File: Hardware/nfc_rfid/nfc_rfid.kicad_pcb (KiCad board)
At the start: 4 copper layers, 74.1 x 32 mm, 158 parts, among them IC1 ST25R3916-AQWT, IC2 FAN48610BUC50X, J1 BW0033AG-L3.4W0.9H1.8, J2 BW0033AG-L3.4W0.9H1.8, J3 HC-FPC-05-09-18RLTAG, J4 +, J5 -, J6 AFH34-S06FIA-1H, J7 BW0033AG-L3.4W0.9H1.8, J8 BW0033AG-L3.4W0.9H1.8, Q1 AO3400A, Q2 DMN2004TK-7, Q3 DMP2004TK-7, Q4 DMN2004TK-7, Q5 DMN5L06TK-7, U1 LMV358AIDGKR, U2 LMV331IDCKR, U3 LMV358AIDGKR, Y1 CF4027M12010001

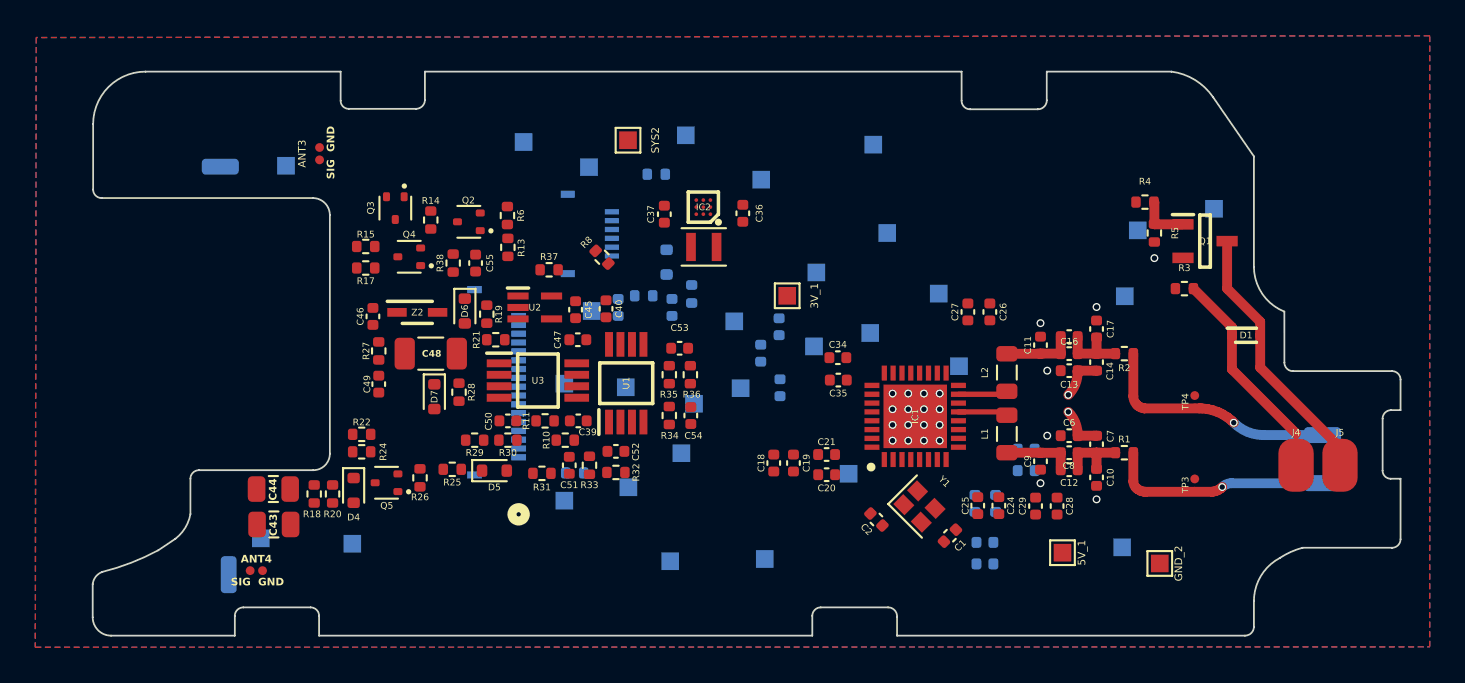
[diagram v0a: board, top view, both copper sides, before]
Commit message: PCB: RFID low freq part done
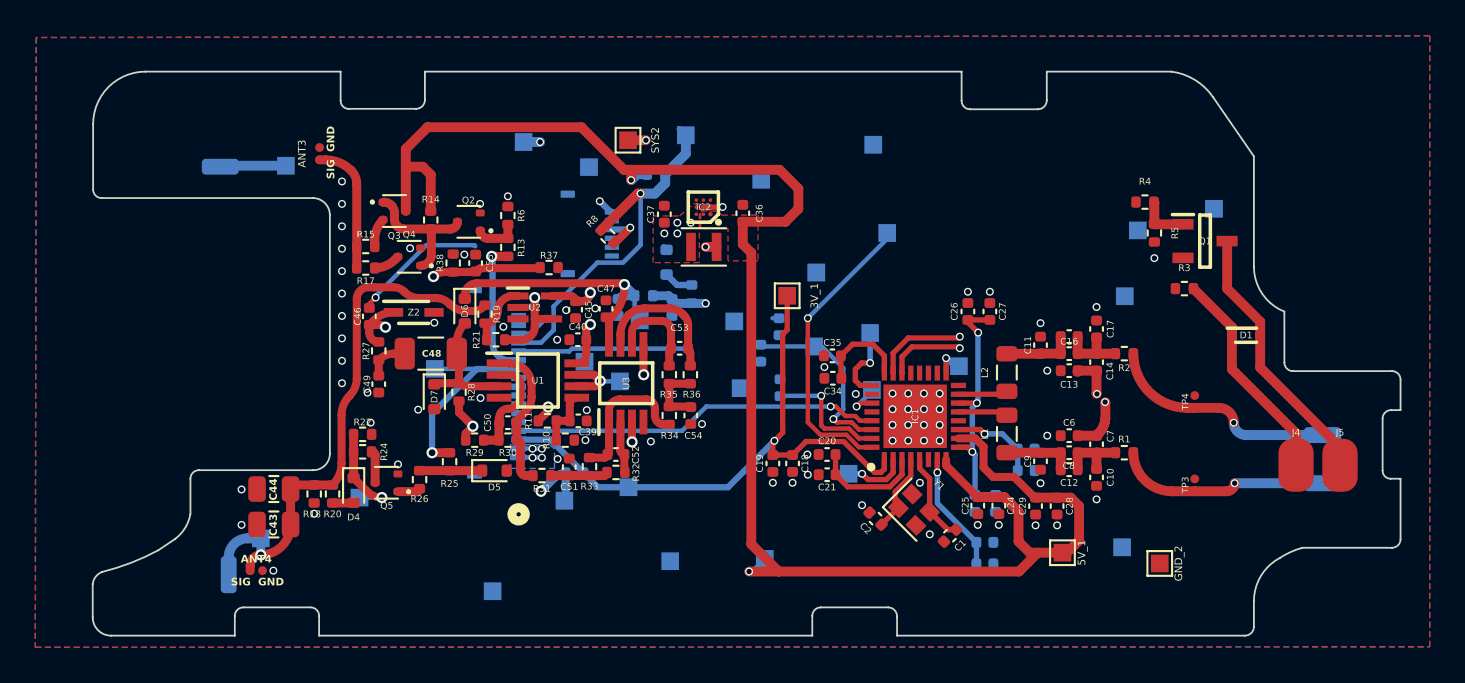
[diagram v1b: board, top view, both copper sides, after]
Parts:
- moved TP16 13.2 mm to (94.2, 76.9)
- moved TP12 7.39 mm to (91.0, 64.3)
- moved TP40 6.64 mm to (115.7, 65.5)
- moved TP15 6.64 mm to (99.4, 63.9)
- moved U1 5.01 mm to (96.8, 65.0), turned to 0 degrees
- moved U3 5.01 mm to (101.8, 65.2), turned to 90 degrees
- moved TP34 2.77 mm to (102.6, 61.6)
- moved TP39 2.65 mm to (86.7, 71.6)
- moved C40 2.37 mm to (99.1, 62.7), turned to 0 degrees
- moved C47 2.37 mm to (100.7, 60.9), turned to -90 degrees
- moved C35 1.41 mm to (113.5, 63.6), turned to 180 degrees
- moved C26 1.24 mm to (121.2, 61.1), turned to 90 degrees
- moved C27 1.24 mm to (122.4, 61.1), turned to 90 degrees
- moved R8 1.24 mm to (100.8, 56.8)
- moved C34 1.20 mm to (113.5, 64.9), turned to 180 degrees
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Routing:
- net +5V: track 0.00 -> 98.5 mm, vias 0 -> 2
- net /Peripheral/RFID_CARRIER: track 0.00 -> 46.6 mm, vias 0 -> 4
- net +3.3V: track 0.00 -> 46.6 mm, vias 0 -> 2
- net Net-(J7-Pin_1): track 0.00 -> 31.6 mm, vias 0 -> 1
- net A+3.3V: track 0.00 -> 29.5 mm, vias 0 -> 4
- net /Peripheral/iBTN: track 0.00 -> 29.0 mm, vias 0 -> 2
- net /NFC/NFC_CS: track 0.00 -> 20.9 mm, vias 0 -> 1
- net +1.65V: track 0.00 -> 17.9 mm, vias 0 -> 4
- net /NFC/SPI_R_MISO: track 0.00 -> 17.2 mm, vias 0 -> 1
- net /NFC/SPI_R_MOSI: track 0.00 -> 17.0 mm, vias 0 -> 1
- net /NFC/RFI_P: track 2.55 -> 17.8 mm, vias 1 -> 2
- net /NFC/RFI_N: track 2.65 -> 17.6 mm, vias 1 -> 2
- net Net-(IC1-VDD_DR): track 0.00 -> 14.7 mm, vias 0 -> 3
- net /Peripheral/RFID_PULL: track 0.00 -> 11.5 mm, vias 0 -> 1
- net Net-(J8-Pin_1): track 0.00 -> 11.3 mm
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- added copper zone on In1.Cu, net +1.65V
- added copper zone on F.Cu, net +5V
- added copper zone on In1.Cu, net A+3.3V
- added copper zone on B.Cu, net SYS
- added copper zone on F.Cu, net SYS
- added copper zone on In1.Cu, net SYS

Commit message: PCB: NFC_RFID layout done
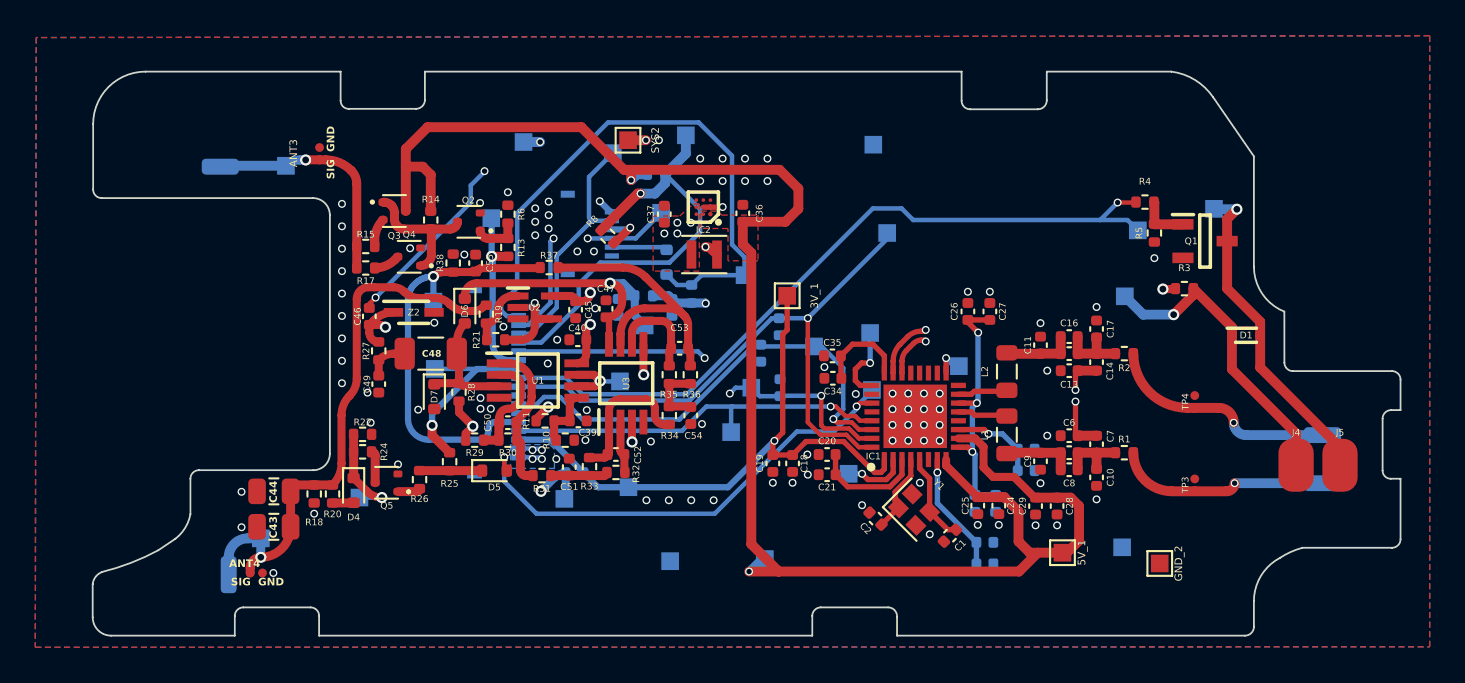
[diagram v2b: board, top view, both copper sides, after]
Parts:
- IC2: value FAN48610BUC50X -> FAN48610UC50X
- moved TP16 16.2 mm to (107.7, 67.9)
- moved TP11 15.0 mm to (94.2, 55.8)
- moved TP15 9.21 mm to (90.9, 60.5)
- moved TP7 5.97 mm to (103.8, 55.5)
- moved TP6 4.07 mm to (108.5, 59.0)
- moved TP8 1.56 mm to (101.0, 52.1)
- moved TP10 0.61 mm to (108.9, 65.4)
- moved L3 0.43 mm to (106.2, 57.9)
- moved TP34 0.40 mm to (102.8, 61.9)
- moved C44 0.13 mm to (81.8, 71.3)
- moved TP38 0.13 mm to (80.8, 75.9)
- moved C43 0.13 mm to (81.8, 73.3)
- moved R11 0.13 mm to (97.2, 67.3)
- moved TP18 0.10 mm to (98.3, 71.7)
- moved R19 0.08 mm to (93.9, 61.2)
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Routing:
- net Net-(J3-Pad10): track 0.00 -> 42.8 mm, vias 0 -> 1
- net /Peripheral/IR_RX: track 1.67 -> 34.0 mm
- net /NFC/NFC_IRQ: track 2.24 -> 27.8 mm, vias 1 -> 2
- net /NFC/SPI_R_MISO: track 17.2 -> 35.4 mm
- net /Peripheral/RFID_RF_IN: track 6.18 -> 24.0 mm
- net /Peripheral/iBTN: track 29.0 -> 45.5 mm, vias 2 -> 3
- net /NFC/SPI_R_SCK: track 10.9 -> 27.0 mm
- net /RFID_iBTN/IR_TX: track 0.00 -> 12.8 mm, vias 0 -> 2
- net /RFID_iBTN/SPEAKER: track 2.02 -> 14.1 mm
- net Net-(C53-Pad2): track 8.07 -> 16.3 mm
- net /NFC/SPI_R_MOSI: track 17.0 -> 24.6 mm, vias 1 -> 3
- net Net-(D1-K): track 12.4 -> 17.6 mm, vias 0 -> 1
- net Net-(D1-A): track 15.3 -> 18.7 mm, vias 0 -> 1
- net /RFID_iBTN/TSOP_RX: track 0.21 -> 3.16 mm
- net /NFC/RFI_P: track 17.8 -> 15.4 mm
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- added copper zone on In2.Cu, net +1.65V
- added copper zone on In2.Cu, net A+3.3V
- added copper zone on In1.Cu, net GND
- added copper zone on In2.Cu, net SYS
- removed copper zone on In1.Cu, net +1.65V
- removed copper zone on In1.Cu, net A+3.3V
- removed copper zone on In2.Cu, net GND
- removed copper zone on In1.Cu, net SYS

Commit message: PCB: nfc_rfid add via
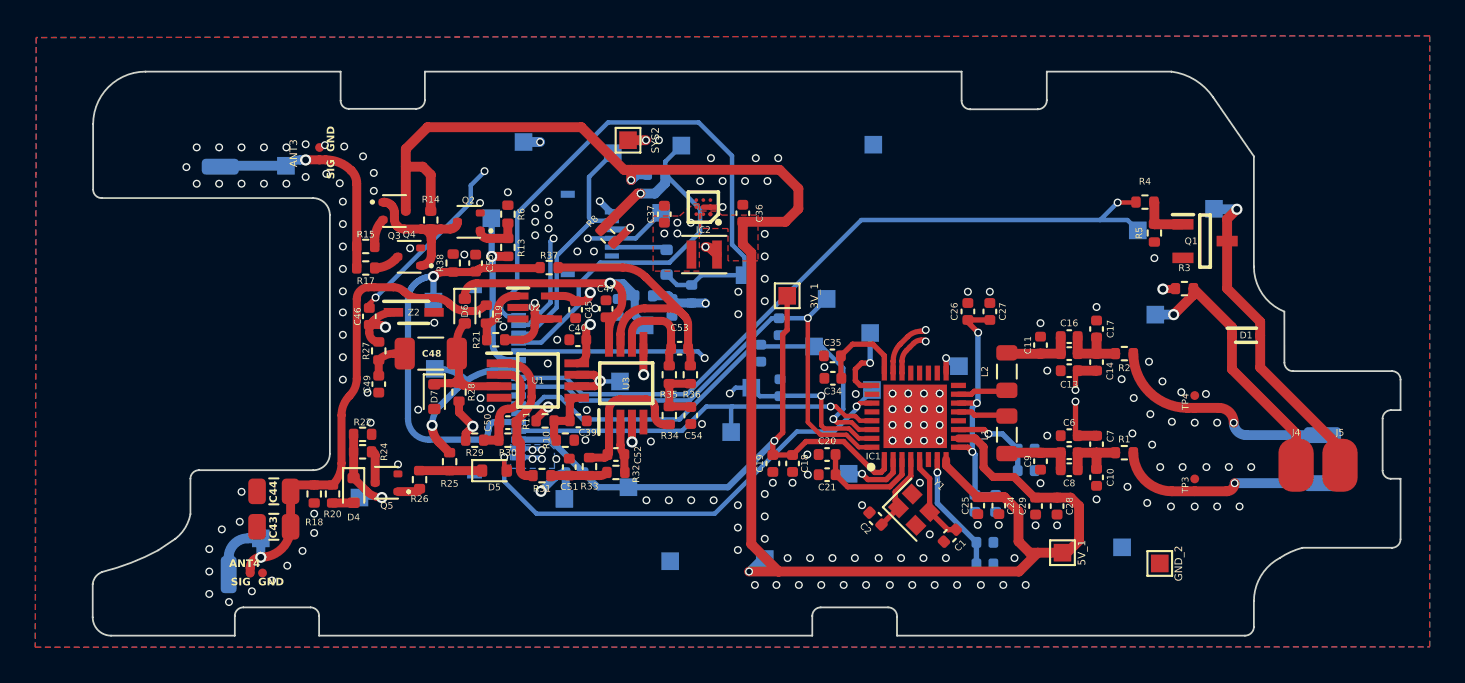
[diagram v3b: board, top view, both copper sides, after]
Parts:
- moved TP13 5.07 mm to (113.2, 60.4)
- moved TP21 2.02 mm to (131.8, 61.3)
- moved TP9 0.64 mm to (104.9, 51.7)
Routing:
- net /NFC/SPI_R_MISO: track 35.4 -> 30.3 mm
- net Net-(D1-K): track 17.6 -> 15.5 mm
- net Net-(Q2-D): track 7.87 -> 9.79 mm
- net Net-(D6-A): track 7.26 -> 9.16 mm
- net /Peripheral/RFID_CARRIER: track 46.1 -> 47.3 mm
- net A+3.3V: track 30.4 -> 31.6 mm
- net /Peripheral/RFID_PULL: track 11.0 -> 10.2 mm
- net /Peripheral/iBTN: track 45.5 -> 44.8 mm
- net Net-(J3-Pad10): track 42.8 -> 42.3 mm
- net GND: vias 93 -> 178

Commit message: PCB: add "remove from bom" entity; adjust design rule
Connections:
- J3 pad 19: (no net) -> GND
- J3 pad 20: (no net) -> GND
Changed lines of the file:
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@@
 		(sheetname "NFC")
 		(sheetfile "nfc.kicad_sch")
-		(attr smd)
+		(attr smd exclude_from_bom)
 		(fp_text user "${REFERENCE}"
 			(at 0 -3.3782 90)
@@
 		(sheetname "Peripheral")
 		(sheetfile "peripheral.kicad_sch")
-		(attr exclude_from_pos_files)
+		(attr exclude_from_pos_files exclude_from_bom)
 		(fp_line
 			(start 0.7 -0.7)
@@
 		(sheetname "NFC")
 		(sheetfile "nfc.kicad_sch")
-		(attr smd)
+		(attr smd exclude_from_bom)
 		(fp_text user "${REFERENCE}"
 			(at 0 -3.3782 90)
@@
 		(sheetname "Peripheral")
 		(sheetfile "peripheral.kicad_sch")
-		(attr exclude_from_pos_files)
+		(attr exclude_from_pos_files exclude_from_bom)
 		(fp_line
 			(start 0.7 -0.7)
@@
 		(sheetname "RFID_iBTN")
 		(sheetfile "RFID_iBTN.kicad_sch")
-		(attr smd)
+		(attr smd exclude_from_bom)
 		(fp_text user "${REFERENCE}"
 			(at 0 -3.3782 90)
@@
 		(sheetname "Peripheral")
 		(sheetfile "peripheral.kicad_sch")
-		(attr exclude_from_pos_files)
+		(attr exclude_from_pos_files exclude_from_bom)
 		(fp_line
 			(start 0.7 -0.7)
@@
 		(sheetname "Peripheral")
 		(sheetfile "peripheral.kicad_sch")
-		(attr exclude_from_pos_files)
+		(attr exclude_from_pos_files exclude_from_bom)
 		(fp_line
 			(start 0.7 -0.7)
@@
 		(sheetname "RFID_iBTN")
 		(sheetfile "RFID_iBTN.kicad_sch")
-		(attr smd)
+		(attr smd exclude_from_bom)
 		(fp_text user "${REFERENCE}"
 			(at 0 -3.3782 0)
@@
 			)
 		)
-		(property "Datasheet" ""
+		(property "Datasheet" "https://datasheet.datasheetarchive.com/originals/distributors/Datasheets_SAMA/df3e85b90ab3bcbb613a20fbddbf2a27.pdf"
 			(at 0 0 0)
 			(layer "F.Fab")
@@
 			)
 		)
-		(property "Mouser Part Number" ""
+		(property "Mouser Part Number" "512-FAN48610BUC50X"
 			(at 0 0 180)
 			(unlocked yes)
@@
 			)
 		)
-		(property "Manufacturer_Part_Number" "FAN48610UC50X"
+		(property "Manufacturer_Part_Number" "FAN48610BUC50X"
 			(at 0 0 180)
 			(unlocked yes)
@@
 		(sheetname "Peripheral")
 		(sheetfile "peripheral.kicad_sch")
-		(attr exclude_from_pos_files)
+		(attr exclude_from_pos_files exclude_from_bom)
 		(fp_line
 			(start 0.7 0.7)
@@
 		(sheetname "NFC")
 		(sheetfile "nfc.kicad_sch")
-		(attr exclude_from_pos_files)
+		(attr exclude_from_pos_files exclude_from_bom)
 		(fp_line
 			(start 0.7 0.7)
@@
 		(sheetname "Peripheral")
 		(sheetfile "peripheral.kicad_sch")
-		(attr exclude_from_pos_files)
+		(attr exclude_from_pos_files exclude_from_bom)
 		(fp_line
 			(start 0.7 0.7)
@@
 		(sheetname "RFID_iBTN")
 		(sheetfile "RFID_iBTN.kicad_sch")
-		(attr exclude_from_pos_files)
+		(attr exclude_from_pos_files exclude_from_bom)
 		(fp_line
 			(start 0.7 0.7)
@@
 		(sheetname "Peripheral")
 		(sheetfile "peripheral.kicad_sch")
-		(attr exclude_from_pos_files)
+		(attr exclude_from_pos_files exclude_from_bom)
 		(fp_line
 			(start 0.7 0.7)
@@
 		(sheetname "Peripheral")
 		(sheetfile "peripheral.kicad_sch")
-		(attr exclude_from_pos_files)
+		(attr exclude_from_pos_files exclude_from_bom)
 		(fp_line
 			(start 0.7 0.7)
@@
 		(sheetname "Peripheral")
 		(sheetfile "peripheral.kicad_sch")
-		(attr exclude_from_pos_files)
+		(attr exclude_from_pos_files exclude_from_bom)
 		(fp_line
 			(start 0.7 0.7)
@@
 			(size 0.4064 0.8382)
 			(layers "B.Cu" "B.Paste" "B.Mask")
+			(net 1 "GND")
+			(pinfunction "19")
+			(pintype "passive")
 		)
 		(pad "20" smd rect
@@
 			(size 0.4064 0.8382)
 			(layers "B.Cu" "B.Paste" "B.Mask")
+			(net 1 "GND")
+			(pinfunction "20")
+			(pintype "passive")
 		)
 	)
@@
 		(sheetname "Peripheral")
 		(sheetfile "peripheral.kicad_sch")
-		(attr exclude_from_pos_files)
+		(attr exclude_from_pos_files exclude_from_bom)
 		(fp_line
 			(start 0.7 0.7)
@@
 		(sheetname "Peripheral")
 		(sheetfile "peripheral.kicad_sch")
-		(attr exclude_from_pos_files)
+		(attr exclude_from_pos_files exclude_from_bom)
 		(fp_line
 			(start 0.7 0.7)
@@
 		(sheetname "RFID_iBTN")
 		(sheetfile "RFID_iBTN.kicad_sch")
-		(attr exclude_from_pos_files)
+		(attr exclude_from_pos_files exclude_from_bom)
 		(fp_line
 			(start -0.7 0.7)
@@
 		(sheetname "RFID_iBTN")
 		(sheetfile "RFID_iBTN.kicad_sch")
-		(attr exclude_from_pos_files)
+		(attr exclude_from_pos_files exclude_from_bom)
 		(fp_line
 			(start -0.7 0.7)
@@
 		(sheetname "Peripheral")
 		(sheetfile "peripheral.kicad_sch")
-		(attr exclude_from_pos_files)
+		(attr exclude_from_pos_files exclude_from_bom)
 		(fp_line
 			(start 0.7 0.7)
@@
 		(sheetname "Peripheral")
 		(sheetfile "peripheral.kicad_sch")
-		(attr exclude_from_pos_files)
+		(attr exclude_from_pos_files exclude_from_bom)
 		(fp_line
 			(start 0.7 0.7)
@@
 		(sheetname "Peripheral")
 		(sheetfile "peripheral.kicad_sch")
-		(attr exclude_from_pos_files)
+		(attr exclude_from_pos_files exclude_from_bom)
 		(fp_line
 			(start 0.7 0.7)
@@
 		(sheetname "Peripheral")
 		(sheetfile "peripheral.kicad_sch")
-		(attr exclude_from_pos_files)
+		(attr exclude_from_pos_files exclude_from_bom)
 		(fp_line
 			(start 0.7 0.7)
@@
 		(sheetname "Peripheral")
 		(sheetfile "peripheral.kicad_sch")
-		(attr exclude_from_pos_files)
+		(attr exclude_from_pos_files exclude_from_bom)
 		(fp_line
 			(start 0.7 0.7)
@@
 		(sheetname "RFID_iBTN")
 		(sheetfile "RFID_iBTN.kicad_sch")
-		(attr exclude_from_pos_files)
+		(attr exclude_from_pos_files exclude_from_bom)
 		(fp_line
 			(start 0.7 0.7)
@@
 		(sheetname "Peripheral")
 		(sheetfile "peripheral.kicad_sch")
-		(attr exclude_from_pos_files)
+		(attr exclude_from_pos_files exclude_from_bom)
 		(fp_line
 			(start 0.7 0.7)
@@
 		(sheetname "NFC")
 		(sheetfile "nfc.kicad_sch")
-		(attr exclude_from_pos_files)
+		(attr exclude_from_pos_files exclude_from_bom)
 		(fp_line
 			(start 0.7 0.7)
@@
 		(sheetname "Peripheral")
 		(sheetfile "peripheral.kicad_sch")
-		(attr exclude_from_pos_files)
+		(attr exclude_from_pos_files exclude_from_bom)
 		(fp_line
 			(start 0.7 0.7)
@@
 		(sheetname "RFID_iBTN")
 		(sheetfile "RFID_iBTN.kicad_sch")
-		(attr exclude_from_pos_files)
+		(attr exclude_from_pos_files exclude_from_bom)
 		(fp_line
 			(start 0.7 0.7)
@@
 		(sheetname "Peripheral")
 		(sheetfile "peripheral.kicad_sch")
-		(attr exclude_from_pos_files)
+		(attr exclude_from_pos_files exclude_from_bom)
 		(fp_line
 			(start 0.7 0.7)
@@
 		(sheetname "Peripheral")
 		(sheetfile "peripheral.kicad_sch")
-		(attr exclude_from_pos_files)
+		(attr exclude_from_pos_files exclude_from_bom)
 		(fp_line
 			(start 0.7 0.7)
@@
 		(sheetname "RFID_iBTN")
 		(sheetfile "RFID_iBTN.kicad_sch")
-		(attr exclude_from_pos_files)
+		(attr exclude_from_pos_files exclude_from_bom)
 		(fp_line
 			(start 0.7 0.7)
@@
 		(sheetname "Peripheral")
 		(sheetfile "peripheral.kicad_sch")
-		(attr exclude_from_pos_files)
+		(attr exclude_from_pos_files exclude_from_bom)
 		(fp_line
 			(start 0.7 0.7)
@@
 		(sheetname "Peripheral")
 		(sheetfile "peripheral.kicad_sch")
-		(attr exclude_from_pos_files)
+		(attr exclude_from_pos_files exclude_from_bom)
 		(fp_line
 			(start 0.7 0.7)
@@
 		(sheetname "Peripheral")
 		(sheetfile "peripheral.kicad_sch")
-		(attr exclude_from_pos_files)
+		(attr exclude_from_pos_files exclude_from_bom)
 		(fp_line
 			(start 0.7 0.7)
@@
 		(sheetname "NFC")
 		(sheetfile "nfc.kicad_sch")
-		(attr exclude_from_pos_files)
+		(attr exclude_from_pos_files exclude_from_bom)
 		(fp_line
 			(start 0.7 0.7)
@@
 		(sheetname "Peripheral")
 		(sheetfile "peripheral.kicad_sch")
-		(attr exclude_from_pos_files)
+		(attr exclude_from_pos_files exclude_from_bom)
 		(fp_line
 			(start 0.7 0.7)
@@
 		(sheetname "Peripheral")
 		(sheetfile "peripheral.kicad_sch")
-		(attr exclude_from_pos_files)
+		(attr exclude_from_pos_files exclude_from_bom)
 		(fp_line
 			(start 0.7 0.7)
